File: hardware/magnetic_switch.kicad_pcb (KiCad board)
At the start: 2 copper layers, 15 x 10 mm, 20 parts, among them J1 V_IN, J2 GND_IN, J3 V_OUT, J4 GND_OUT, Q1 DMP2040UFDF, Q3 DMP2040UFDF, Q4 RUM002N02T2L, U1 DRV5012, U3 TPS70933, U4 SN74AUP1G74

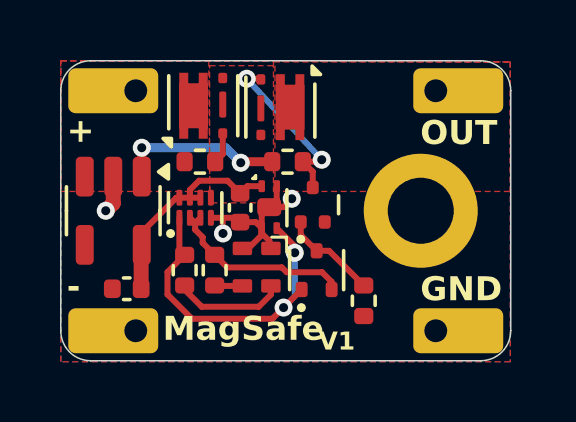
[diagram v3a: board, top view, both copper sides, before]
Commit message: added missing via on R1 gnd
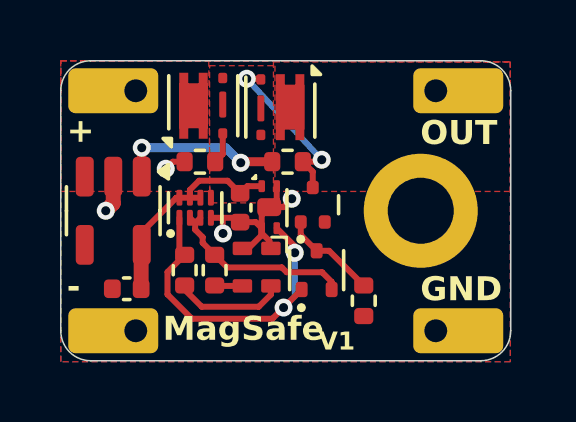
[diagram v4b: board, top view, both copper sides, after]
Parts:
- R4: value 1k -> 100
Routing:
- net GND: track 7.94 -> 8.66 mm, vias 3 -> 4
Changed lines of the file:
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@@
 			)
 		)
+		(model "${KICAD9_3DMODEL_DIR}/Package_DFN_QFN.3dshapes/DFN-6-1EP_2x2mm_P0.5mm_EP0.61x1.42mm.step"
+			(offset
+				(xyz 0 0 0)
+			)
+			(scale
+				(xyz 1 1 1)
+			)
+			(rotate
+				(xyz 0 0 0)
+			)
+		)
 	)
 	(footprint "Package_TO_SOT_SMD:Vishay_PowerPAK_SC70-6L_Single"
@@
 			)
 		)
+		(model "${KICAD9_3DMODEL_DIR}/Package_DFN_QFN.3dshapes/DFN-6-1EP_2x2mm_P0.5mm_EP0.61x1.42mm.step"
+			(offset
+				(xyz 0 0 0)
+			)
+			(scale
+				(xyz 1 1 1)
+			)
+			(rotate
+				(xyz 0 0 0)
+			)
+		)
 	)
 	(footprint "Package_TO_SOT_SMD:SOT-23-5"
@@
 			)
 		)
-		(property "Value" "1k"
+		(property "Value" "100"
 			(at 0 1.17 90)
 			(layer "F.Fab")
@@
 			)
 		)
+		(model "${KICAD9_3DMODEL_DIR}/Package_TO_SOT_SMD.3dshapes/SOT-323_SC-70.step"
+			(offset
+				(xyz 0 0 0)
+			)
+			(scale
+				(xyz 0.75 0.75 0.75)
+			)
+			(rotate
+				(xyz -0 -0 -0)
+			)
+		)
 	)
 	(footprint "Footprints:WireSolderPad_w_hole"
@@
 		)
 		(embedded_fonts no)
+		(model "${KICAD9_3DMODEL_DIR}/LED_SMD.3dshapes/LED_RGB_1210.step"
+			(offset
+				(xyz 0 0 0)
+			)
+			(scale
+				(xyz 0.45 0.55 0.5)
+			)
+			(rotate
+				(xyz -0 -0 -0)
+			)
+		)
 	)
 	(footprint "Footprints:WireSolderPad_w_hole"
@@
 			)
 		)
+		(model "${KICAD9_3DMODEL_DIR}/Package_TO_SOT_SMD.3dshapes/SOT-323_SC-70.step"
+			(offset
+				(xyz 0 0 0)
+			)
+			(scale
+				(xyz 0.7 0.6 0.6)
+			)
+			(rotate
+				(xyz -0 -0 -0)
+			)
+		)
 	)
 	(footprint "Resistor_SMD:R_0402_1005Metric"
@@
 		)
 		(embedded_fonts no)
+		(model "${KICAD9_3DMODEL_DIR}/Package_SON.3dshapes/X2SON-8_1.4x1mm_P0.35mm.step"
+			(offset
+				(xyz 0 0 0)
+			)
+			(scale
+				(xyz 1 1 1)
+			)
+			(rotate
+				(xyz 0 0 0)
+			)
+		)
 	)
 	(footprint "Package_SON:X2SON-8_1.4x1mm_P0.35mm"
@@
 	)
 	(segment
+		(start 129.911 74.057)
+		(end 129.676 74.292)
+		(width 0.2)
+		(layer "F.Cu")
+		(net 1)
+	)
+	(segment
 		(start 132.431 76.947)
 		(end 132.231 76.947)
@@
 	)
 	(segment
+		(start 130.304 74.057)
+		(end 129.911 74.057)
+		(width 0.2)
+		(layer "F.Cu")
+		(net 1)
+	)
+	(segment
 		(start 132.156 76.072)
 		(end 132.675 76.072)
@@
 		(size 0.6)
 		(drill 0.3)
+		(layers "F.Cu" "B.Cu")
+		(net 1)
+	)
+	(via
+		(at 129.676 74.292)
+		(size 0.6)
+		(drill 0.3)
